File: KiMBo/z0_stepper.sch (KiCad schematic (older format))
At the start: 25 parts, among them U23 TMC2130

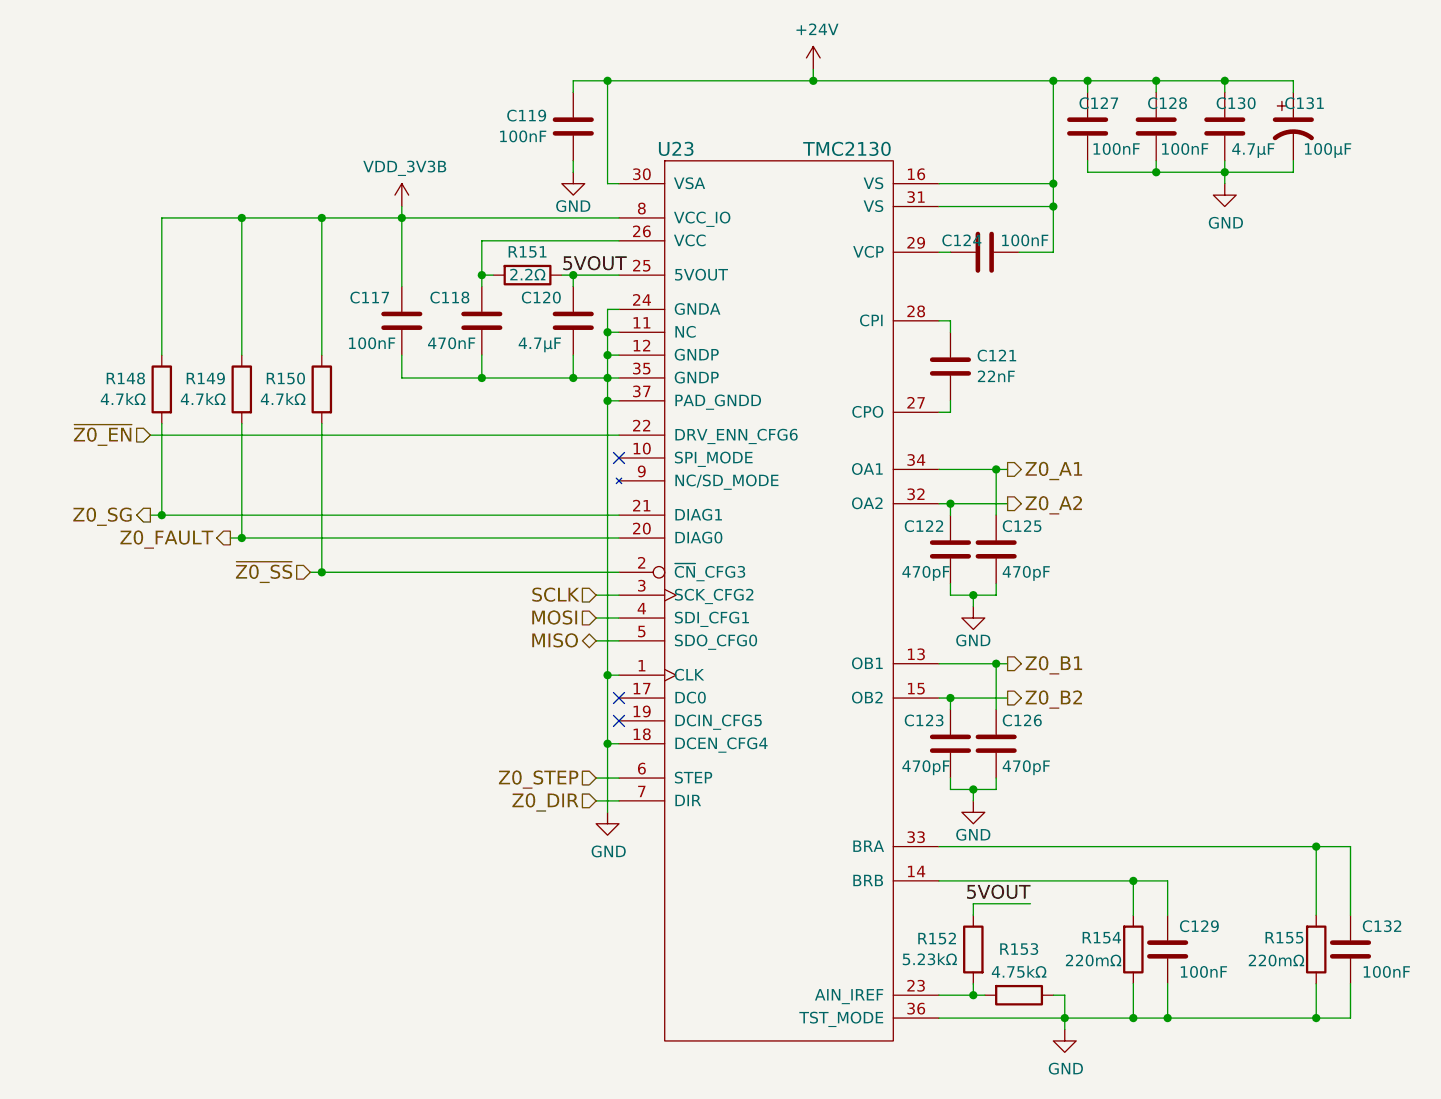
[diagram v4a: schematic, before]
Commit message: Add equivalent annotations document, associate more footprints
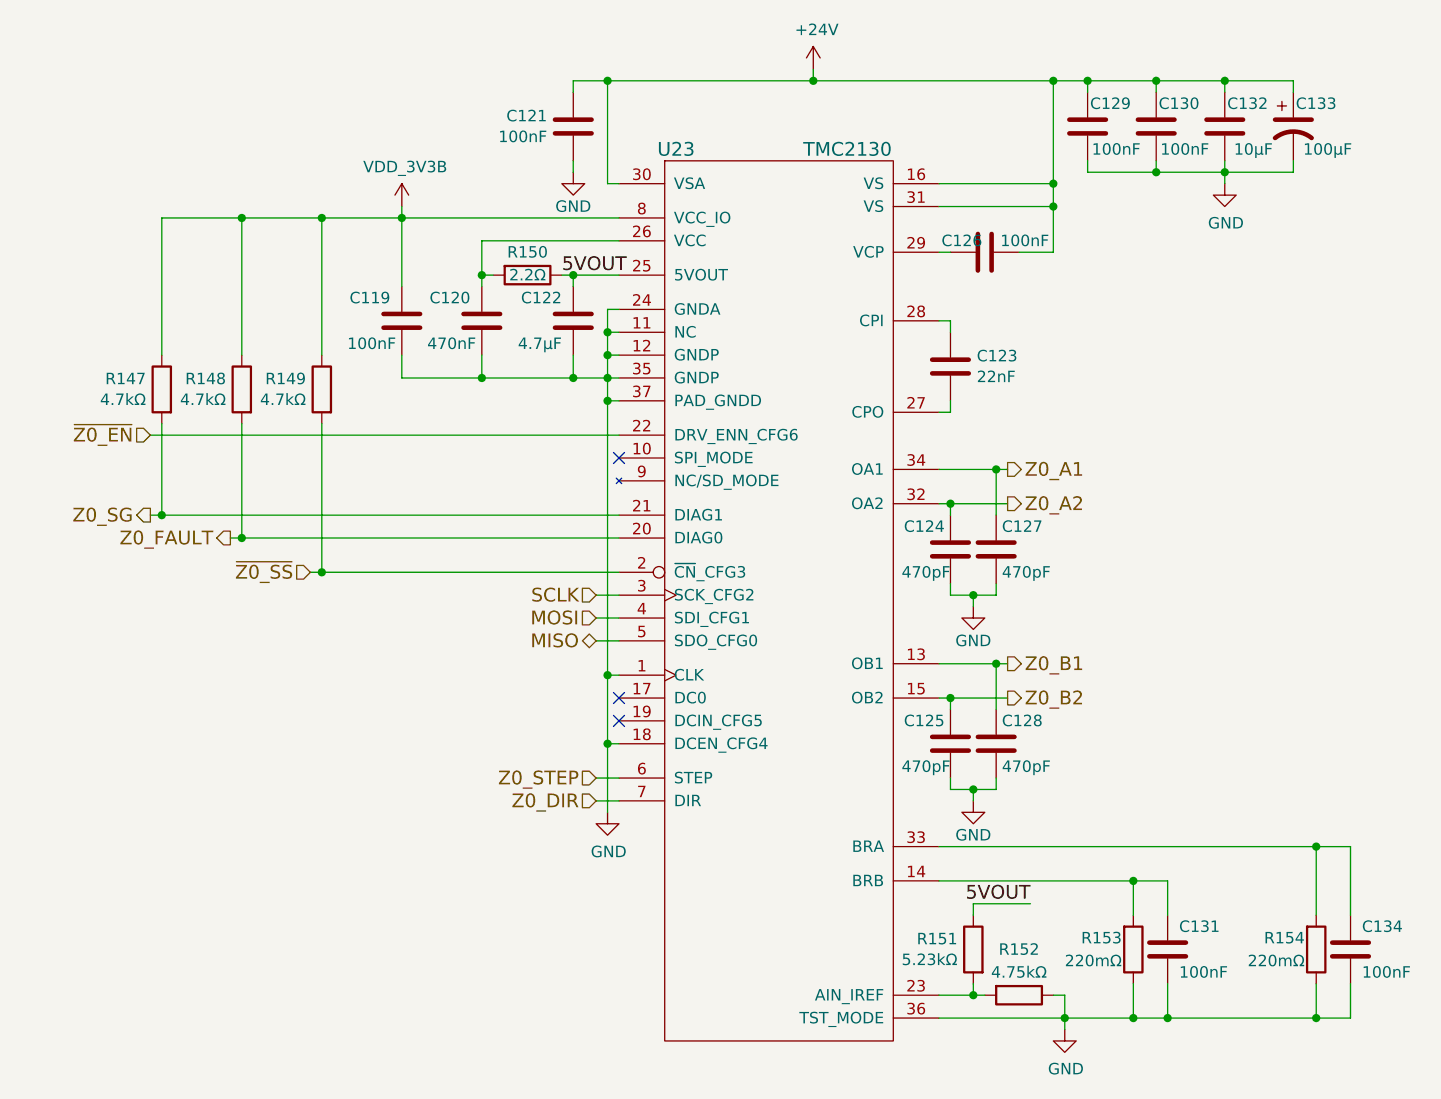
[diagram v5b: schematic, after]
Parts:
- C119: renamed from C117; footprint (none) -> Capacitors_SMD:C_0603
- C120: renamed from C118; footprint (none) -> Capacitors_SMD:C_0603
- C121: renamed from C119; footprint (none) -> Capacitors_SMD:C_0603
- C122: renamed from C120; footprint (none) -> Capacitors_SMD:C_0402
- C123: renamed from C121; footprint (none) -> Capacitors_SMD:C_0402
- C124: renamed from C122; footprint (none) -> Capacitors_SMD:C_0603
- C125: renamed from C123; footprint (none) -> Capacitors_SMD:C_0603
- C126: renamed from C124; footprint (none) -> Capacitors_SMD:C_0603
- C127: renamed from C125; footprint (none) -> Capacitors_SMD:C_0603
- C128: renamed from C126; footprint (none) -> Capacitors_SMD:C_0603
- C129: renamed from C127; footprint (none) -> Capacitors_SMD:C_0603
- C130: renamed from C128; footprint (none) -> Capacitors_SMD:C_0603
- C131: renamed from C129; footprint (none) -> Capacitors_SMD:C_0603
- C132: renamed from C130; value 4.7μF -> 10μF; footprint (none) -> Capacitors_SMD:C_0805
- C133: renamed from C131; footprint (none) -> Capacitors_SMD:c_elec_8x10
- C134: renamed from C132; footprint (none) -> Capacitors_SMD:C_0603
- renumbered R148 to R147, R149 to R148, R150 to R149, R151 to R150, R152 to R151, R153 to R152, R154 to R153, R155 to R154
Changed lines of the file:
@@
 Z0_SG
 $Comp
-L C C119
+L C C121
 U 1 1 58C0C3C9
 P 7100 3150
-F 0 "C119" H 6986 3104 50  0000 R CNN
+F 0 "C121" H 6986 3104 50  0000 R CNN
 F 1 "100nF" H 6986 3195 50  0000 R CNN
-F 2 "" H 7138 3000 50  0001 C CNN
+F 2 "Capacitors_SMD:C_0603" H 7138 3000 50  0001 C CNN
 F 3 "" H 7100 3150 50  0000 C CNN
 	1    7100 3150
@@
 $EndComp
 $Comp
-L C C124
+L C C126
 U 1 1 58C0C3D0
 P 8900 3700
-F 0 "C124" V 8850 3600 50  0000 C CNN
+F 0 "C126" V 8850 3600 50  0000 C CNN
 F 1 "100nF" V 8850 3875 50  0000 C CNN
-F 2 "" H 8938 3550 50  0001 C CNN
+F 2 "Capacitors_SMD:C_0603" H 8938 3550 50  0001 C CNN
 F 3 "" H 8900 3700 50  0000 C CNN
 	1    8900 3700
@@
 $EndComp
 $Comp
-L CP1 C131
+L CP1 C133
 U 1 1 58C0C3D7
 P 10250 3150
-F 0 "C131" H 10300 3250 50  0000 C CNN
+F 0 "C133" H 10350 3250 50  0000 C CNN
 F 1 "100μF" H 10400 3050 50  0000 C CNN
-F 2 "" H 10250 3150 50  0001 C CNN
+F 2 "Capacitors_SMD:c_elec_8x10" H 10250 3150 50  0001 C CNN
 F 3 "" H 10250 3150 50  0000 C CNN
 	1    10250 3150
@@
 $EndComp
 $Comp
-L C C127
+L C C129
 U 1 1 58C0C3DE
 P 9350 3150
-F 0 "C127" H 9300 3250 50  0000 C CNN
+F 0 "C129" H 9250 3250 50  0000 C CNN
 F 1 "100nF" H 9225 3050 50  0000 C CNN
-F 2 "" H 9388 3000 50  0001 C CNN
+F 2 "Capacitors_SMD:C_0603" H 9388 3000 50  0001 C CNN
 F 3 "" H 9350 3150 50  0000 C CNN
 	1    9350 3150
@@
 $EndComp
 $Comp
-L GND #PWR0225
+L GND #PWR0226
 U 1 1 58C0C3E5
 P 7100 3350
-F 0 "#PWR0225" H 7100 3100 50  0001 C CNN
+F 0 "#PWR0226" H 7100 3100 50  0001 C CNN
 F 1 "GND" H 7100 3200 50  0000 C CNN
 F 2 "" H 7100 3350 50  0000 C CNN
@@
 $EndComp
 $Comp
-L C C128
+L C C130
 U 1 1 58C0C3EB
 P 9650 3150
-F 0 "C128" H 9600 3250 50  0000 C CNN
+F 0 "C130" H 9550 3250 50  0000 C CNN
 F 1 "100nF" H 9525 3050 50  0000 C CNN
-F 2 "" H 9688 3000 50  0001 C CNN
+F 2 "Capacitors_SMD:C_0603" H 9688 3000 50  0001 C CNN
 F 3 "" H 9650 3150 50  0000 C CNN
 	1    9650 3150
@@
 $EndComp
 $Comp
-L GND #PWR0226
+L GND #PWR0227
 U 1 1 58C0C3F2
 P 9950 3400
-F 0 "#PWR0226" H 9950 3150 50  0001 C CNN
+F 0 "#PWR0227" H 9950 3150 50  0001 C CNN
 F 1 "GND" H 9955 3227 50  0000 C CNN
 F 2 "" H 9950 3400 50  0000 C CNN
@@
 $EndComp
 $Comp
-L +24V #PWR0227
+L +24V #PWR0228
 U 1 1 58C0C3F8
 P 8150 2900
-F 0 "#PWR0227" H 8150 2750 50  0001 C CNN
+F 0 "#PWR0228" H 8150 2750 50  0001 C CNN
 F 1 "+24V" H 8165 3073 50  0000 C CNN
 F 2 "" H 8150 2900 50  0000 C CNN
@@
 $EndComp
 $Comp
-L C C121
+L C C123
 U 1 1 58C0C3FE
 P 8750 4200
-F 0 "C121" H 8865 4246 50  0000 L CNN
+F 0 "C123" H 8865 4246 50  0000 L CNN
 F 1 "22nF" H 8865 4155 50  0000 L CNN
-F 2 "" H 8788 4050 50  0001 C CNN
+F 2 "Capacitors_SMD:C_0402" H 8788 4050 50  0001 C CNN
 F 3 "" H 8750 4200 50  0000 C CNN
 	1    8750 4200
@@
 $EndComp
 $Comp
-L R R155
+L R R154
 U 1 1 58C0C405
 P 10350 6750
-F 0 "R155" H 10300 6700 50  0000 R CNN
+F 0 "R154" H 10300 6700 50  0000 R CNN
 F 1 "220mΩ" H 10300 6800 50  0000 R CNN
 F 2 "" V 10280 6750 50  0001 C CNN
@@
 $EndComp
 $Comp
-L R R154
+L R R153
 U 1 1 58C0C40C
 P 9550 6750
-F 0 "R154" H 9500 6700 50  0000 R CNN
+F 0 "R153" H 9500 6700 50  0000 R CNN
 F 1 "220mΩ" H 9500 6800 50  0000 R CNN
 F 2 "" V 9480 6750 50  0001 C CNN
@@
 $EndComp
 $Comp
-L GND #PWR0228
+L GND #PWR0229
 U 1 1 58C0C413
 P 9250 7100
-F 0 "#PWR0228" H 9250 6850 50  0001 C CNN
+F 0 "#PWR0229" H 9250 6850 50  0001 C CNN
 F 1 "GND" H 9255 6927 50  0000 C CNN
 F 2 "" H 9250 7100 50  0000 C CNN
@@
 NoConn ~ 7300 5650
 $Comp
-L R R151
+L R R150
 U 1 1 58C0C41A
 P 6900 3800
-F 0 "R151" V 6800 3800 50  0000 C CNN
+F 0 "R150" V 6800 3800 50  0000 C CNN
 F 1 "2.2Ω" V 6900 3800 50  0000 C CNN
 F 2 "" V 6830 3800 50  0001 C CNN
@@
 $EndComp
 $Comp
-L C C118
+L C C120
 U 1 1 58C0C421
 P 6700 4000
-F 0 "C118" H 6750 4100 50  0000 L CNN
+F 0 "C120" H 6750 4100 50  0000 L CNN
 F 1 "470nF" H 6725 3900 50  0000 L CNN
-F 2 "" H 6738 3850 50  0001 C CNN
+F 2 "Capacitors_SMD:C_0603" H 6738 3850 50  0001 C CNN
 F 3 "" H 6700 4000 50  0000 C CNN
 	1    6700 4000
@@
 NoConn ~ 7300 5750
 $Comp
-L GND #PWR0229
+L GND #PWR0230
 U 1 1 58C0C436
 P 7250 6150
-F 0 "#PWR0229" H 7250 5900 50  0001 C CNN
+F 0 "#PWR0230" H 7250 5900 50  0001 C CNN
 F 1 "GND" H 7255 5977 50  0000 C CNN
 F 2 "" H 7250 6150 50  0000 C CNN
@@
 $EndComp
 $Comp
-L C C129
+L C C131
 U 1 1 58C0C43C
 P 9700 6750
-F 0 "C129" H 9750 6850 50  0000 L CNN
+F 0 "C131" H 9750 6850 50  0000 L CNN
 F 1 "100nF" H 9750 6650 50  0000 L CNN
-F 2 "" H 9738 6600 50  0001 C CNN
+F 2 "Capacitors_SMD:C_0603" H 9738 6600 50  0001 C CNN
 F 3 "" H 9700 6750 50  0000 C CNN
 	1    9700 6750
@@
 Z0_FAULT
 $Comp
-L R R149
+L R R148
 U 1 1 58C0C444
 P 5650 4300
-F 0 "R149" H 5719 4346 50  0000 L CNN
+F 0 "R148" H 5719 4346 50  0000 L CNN
 F 1 "4.7kΩ" H 5719 4255 50  0000 L CNN
 F 2 "" V 5580 4300 50  0001 C CNN
@@
 NoConn ~ 7300 4600
 $Comp
-L C C120
+L C C122
 U 1 1 58C0C44E
 P 7100 4000
-F 0 "C120" H 7150 4100 50  0000 L CNN
+F 0 "C122" H 7150 4100 50  0000 L CNN
 F 1 "4.7μF" H 7150 3900 50  0000 L CNN
-F 2 "" H 7138 3850 50  0001 C CNN
+F 2 "Capacitors_SMD:C_0402" H 7138 3850 50  0001 C CNN
 F 3 "" H 7100 4000 50  0000 C CNN
 	1    7100 4000
@@
 5VOUT
 $Comp
-L R R152
+L R R151
 U 1 1 58C0C456
 P 8850 6750
-F 0 "R152" H 8919 6796 50  0000 L CNN
+F 0 "R151" H 8919 6796 50  0000 L CNN
 F 1 "5.23kΩ" H 8919 6705 50  0000 L CNN
 F 2 "" V 8780 6750 50  0001 C CNN
@@
 5VOUT
 $Comp
-L R R153
+L R R152
 U 1 1 58C0C45E
 P 9050 6950
-F 0 "R153" V 8850 6950 50  0000 C CNN
+F 0 "R152" V 8850 6950 50  0000 C CNN
 F 1 "4.75kΩ" V 8950 6950 50  0000 C CNN
 F 2 "" V 8980 6950 50  0001 C CNN
@@
 $EndComp
 $Comp
-L R R150
+L R R149
 U 1 1 58C0C465
 P 6000 4300
-F 0 "R150" H 6069 4346 50  0000 L CNN
+F 0 "R149" H 6069 4346 50  0000 L CNN
 F 1 "4.7kΩ" H 6069 4255 50  0000 L CNN
 F 2 "" V 5930 4300 50  0001 C CNN
@@
 $EndComp
 $Comp
-L C C132
+L C C134
 U 1 1 58C0C46C
 P 10500 6750
-F 0 "C132" H 10550 6850 50  0000 L CNN
+F 0 "C134" H 10550 6850 50  0000 L CNN
 F 1 "100nF" H 10550 6650 50  0000 L CNN
-F 2 "" H 10538 6600 50  0001 C CNN
+F 2 "Capacitors_SMD:C_0603" H 10538 6600 50  0001 C CNN
 F 3 "" H 10500 6750 50  0000 C CNN
 	1    10500 6750
@@
 $EndComp
 $Comp
-L C C122
+L C C124
 U 1 1 58C0C473
 P 8750 5000
-F 0 "C122" H 8775 5100 50  0000 L CNN
+F 0 "C124" H 8775 5100 50  0000 L CNN
 F 1 "470pF" H 8750 4900 50  0000 L CNN
-F 2 "" H 8788 4850 50  0001 C CNN
+F 2 "Capacitors_SMD:C_0603" H 8788 4850 50  0001 C CNN
 F 3 "" H 8750 5000 50  0000 C CNN
 	1    8750 5000
@@
 $EndComp
 $Comp
-L GND #PWR0230
+L GND #PWR0231
 U 1 1 58C0C47A
 P 8850 5250
-F 0 "#PWR0230" H 8850 5000 50  0001 C CNN
+F 0 "#PWR0231" H 8850 5000 50  0001 C CNN
 F 1 "GND" H 8850 5100 50  0000 C CNN
 F 2 "" H 8850 5250 50  0000 C CNN
@@
 $EndComp
 $Comp
-L C C125
+L C C127
 U 1 1 58C0C480
 P 8950 5000
-F 0 "C125" H 8975 5100 50  0000 L CNN
+F 0 "C127" H 8975 5100 50  0000 L CNN
 F 1 "470pF" H 8975 4900 50  0000 L CNN
-F 2 "" H 8988 4850 50  0001 C CNN
+F 2 "Capacitors_SMD:C_0603" H 8988 4850 50  0001 C CNN
 F 3 "" H 8950 5000 50  0000 C CNN
 	1    8950 5000
@@
 $EndComp
 $Comp
-L C C123
+L C C125
 U 1 1 58C0C487
 P 8750 5850
-F 0 "C123" H 8775 5950 50  0000 L CNN
+F 0 "C125" H 8775 5950 50  0000 L CNN
 F 1 "470pF" H 8750 5750 50  0000 L CNN
-F 2 "" H 8788 5700 50  0001 C CNN
+F 2 "Capacitors_SMD:C_0603" H 8788 5700 50  0001 C CNN
 F 3 "" H 8750 5850 50  0000 C CNN
 	1    8750 5850
@@
 $EndComp
 $Comp
-L GND #PWR0231
+L GND #PWR0232
 U 1 1 58C0C48E
 P 8850 6100
-F 0 "#PWR0231" H 8850 5850 50  0001 C CNN
+F 0 "#PWR0232" H 8850 5850 50  0001 C CNN
 F 1 "GND" H 8850 5950 50  0000 C CNN
 F 2 "" H 8850 6100 50  0000 C CNN
@@
 $EndComp
 $Comp
-L C C126
+L C C128
 U 1 1 58C0C494
 P 8950 5850
-F 0 "C126" H 8975 5950 50  0000 L CNN
+F 0 "C128" H 8975 5950 50  0000 L CNN
 F 1 "470pF" H 8975 5750 50  0000 L CNN
-F 2 "" H 8988 5700 50  0001 C CNN
+F 2 "Capacitors_SMD:C_0603" H 8988 5700 50  0001 C CNN
 F 3 "" H 8950 5850 50  0000 C CNN
 	1    8950 5850
@@
 	8750 6050 8750 6000
 $Comp
-L R R148
+L R R147
 U 1 1 58C0C50F
 P 5300 4300
-F 0 "R148" H 5369 4346 50  0000 L CNN
+F 0 "R147" H 5369 4346 50  0000 L CNN
 F 1 "4.7kΩ" H 5369 4255 50  0000 L CNN
 F 2 "" V 5230 4300 50  0001 C CNN
@@
 Connection ~ 5650 3550
 $Comp
-L C C130
+L C C132
 U 1 1 58C0C51A
 P 9950 3150
-F 0 "C130" H 9900 3250 50  0000 C CNN
-F 1 "4.7μF" H 9825 3050 50  0000 C CNN
-F 2 "" H 9988 3000 50  0001 C CNN
+F 0 "C132" H 9850 3250 50  0000 C CNN
+F 1 "10μF" H 9825 3050 50  0000 C CNN
+F 2 "Capacitors_SMD:C_0805" H 9988 3000 50  0001 C CNN
 F 3 "" H 9950 3150 50  0000 C CNN
 	1    9950 3150
@@
 	5300 3550 7300 3550
 $Comp
-L VDD_3V3B #PWR0232
+L VDD_3V3B #PWR0233
 U 1 1 5A313878
 P 6350 3500
-F 0 "#PWR0232" H 6350 3350 50  0001 C CNN
+F 0 "#PWR0233" H 6350 3350 50  0001 C CNN
 F 1 "VDD_3V3B" H 6365 3673 50  0000 C CNN
 F 2 "" H 6350 3500 50  0000 C CNN
@@
 $EndComp
 $Comp
-L C C117
+L C C119
 U 1 1 5A89B9DA
 P 6350 4000
-F 0 "C117" H 6400 4100 50  0000 L CNN
+F 0 "C119" H 6400 4100 50  0000 L CNN
 F 1 "100nF" H 6375 3900 50  0000 L CNN
-F 2 "" H 6388 3850 50  0001 C CNN
+F 2 "Capacitors_SMD:C_0603" H 6388 3850 50  0001 C CNN
 F 3 "" H 6350 4000 50  0000 C CNN
 	1    6350 4000
